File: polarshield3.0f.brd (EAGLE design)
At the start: 81.1 x 66 mm, 43 parts, among them Q4 BSS138, Q5 BSS138, Q6 BSS138, Q7 BSS138

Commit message: Added part number GF1A-E3/67A to D1, #1
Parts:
- D1: value (none) -> GF1A-E3/67A
- moved R9 6.00 mm to (23.0, 37.0)
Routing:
- net GND: track 316.7 -> 264.7 mm, vias 17 -> 13
- net M2_EN: track 82.8 -> 72.8 mm
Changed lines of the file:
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@@
 <attribute name="VALUE" x="32.73" y="60.46" size="1.27" layer="27"/>
 </element>
-<element name="D1" library="diode" package="DO214BA" value="" x="17.6" y="27" rot="R90"/>
+<element name="D1" library="diode" package="DO214BA" value="GF1A-E3/67A " x="17.6" y="27" rot="R90"/>
 <element name="MOTOR_2" library="sandy" package="A4988BREAKOUT" value="A4988BREAKOUT" x="20" y="52"/>
 <element name="SJ4" library="polargraph3" package="SJ_2S-NO" value="SOLDERJUMPERNO" x="27" y="43" smashed="yes" rot="MR270"/>
 <element name="SJ5" library="polargraph3" package="SJ_2S-TRACE" value="SOLDERJUMPERTRACE" x="24" y="43" smashed="yes" rot="MR270"/>
 <element name="SJ6" library="polargraph3" package="SJ_2S-TRACE" value="SOLDERJUMPERTRACE" x="21" y="43" smashed="yes" rot="MR270"/>
-<element name="R9" library="resistor" package="M0805" value="10k" x="29" y="37"/>
+<element name="R9" library="resistor" package="M0805" value="10k" x="23" y="37"/>
 <element name="C7" library="resistor" package="C0805" value="100nF" x="16" y="47" rot="R90"/>
 <element name="C8" library="resistor" package="153CLV-0605" value="100uF" x="23" y="47" rot="R180"/>
@@
 <wire x1="22.6" y1="49.8" x2="22.9" y2="49.8" width="1.27" layer="1"/>
 <wire x1="22.9" y1="49.8" x2="25.7" y2="47" width="1.27" layer="1"/>
-<wire x1="25.7" y1="47" x2="27.6" y2="47" width="1.27" layer="1"/>
-<wire x1="27.6" y1="47" x2="33.5" y2="47" width="1.27" layer="1"/>
-<wire x1="33.5" y1="47" x2="36.7" y2="50.2" width="1.27" layer="1"/>
-<wire x1="36.7" y1="50.2" x2="36.7" y2="53.08" width="1.27" layer="1"/>
-<wire x1="36.7" y1="53.08" x2="36.51" y2="53.27" width="1.27" layer="1"/>
 <wire x1="42" y1="47.95" x2="42" y2="53.1" width="1.27" layer="1"/>
 <wire x1="42" y1="53.1" x2="36.68" y2="53.1" width="1.27" layer="1"/>
@@
 <contactref element="CN2" pad="8"/>
 <contactref element="CN2" pad="4"/>
-<wire x1="24.125" y1="37.25" x2="23.875" y2="37" width="0.3048" layer="1"/>
-<wire x1="25.125" y1="37" x2="24.125" y2="37.25" width="0.3048" layer="1"/>
-<wire x1="20.125" y1="32" x2="25.125" y2="37" width="0.8128" layer="1"/>
-<wire x1="17" y1="32" x2="20.125" y2="32" width="0.3048" layer="1"/>
+<wire x1="17" y1="32" x2="20.125" y2="30" width="0.3048" layer="1"/>
 <wire x1="17" y1="34" x2="17" y2="32" width="0.3048" layer="1"/>
 <wire x1="17" y1="34" x2="16.95" y2="34" width="0.3048" layer="1"/>
@@
 <wire x1="19.9" y1="27.3" x2="20.125" y2="27.525" width="0.6096" layer="1"/>
 <wire x1="20.125" y1="27.525" x2="20.125" y2="28.2" width="0.6096" layer="1"/>
-<wire x1="20.125" y1="28.2" x2="20.125" y2="32" width="0.6096" layer="1"/>
+<wire x1="20.125" y1="28.2" x2="20.125" y2="30" width="0.6096" layer="1"/>
 <wire x1="27.28" y1="28.4" x2="27.08" y2="28.2" width="0.254" layer="16"/>
 <wire x1="27.08" y1="28.2" x2="20.125" y2="28.2" width="0.254" layer="16"/>
 <via x="20.125" y="28.2" extent="1-16" drill="0.3048"/>
-<via x="25" y="37" extent="1-16" drill="0.3048"/>
-<via x="35.3" y="38.5" extent="1-16" drill="0.3048"/>
-<wire x1="25.125" y1="37" x2="25" y2="37" width="0.254" layer="1"/>
-<wire x1="35.3" y1="38.5" x2="35.2" y2="38.6" width="0.254" layer="16"/>
-<wire x1="35.2" y1="38.6" x2="35.2" y2="46.1" width="0.254" layer="16"/>
-<wire x1="25" y1="37" x2="31.4" y2="37" width="0.254" layer="16"/>
-<via x="31.4" y="37" extent="1-16" drill="0.3048"/>
-<wire x1="31.4" y1="37" x2="33.8" y2="37" width="0.254" layer="1"/>
-<wire x1="33.8" y1="37" x2="35.3" y2="38.5" width="0.254" layer="1"/>
-<wire x1="35.2" y1="46.1" x2="34.7" y2="46.6" width="0.254" layer="16"/>
-<via x="34.7" y="46.6" extent="1-16" drill="0.3048"/>
-<wire x1="34.7" y1="46.6" x2="28" y2="46.6" width="0.254" layer="1"/>
-<wire x1="28" y1="46.6" x2="27.6" y2="47" width="0.254" layer="1"/>
 <contactref element="CN1" pad="8"/>
 <contactref element="CN1" pad="4"/>
@@
 <wire x1="33.0327" y1="63.0936" x2="32.95" y2="63" width="0.6096" layer="1"/>
 <wire x1="37.9476" y1="63.0936" x2="37.95" y2="63" width="0.6096" layer="1"/>
-<wire x1="30.0609" y1="38.8907" x2="30.0609" y2="37.0332" width="0.6096" layer="1"/>
-<wire x1="30.0609" y1="40.005" x2="30.0609" y2="38.8907" width="0.6096" layer="16"/>
-<wire x1="30.1752" y1="40.1193" x2="30.0609" y2="40.005" width="0.6096" layer="16"/>
-<wire x1="30.1752" y1="41.148" x2="30.1752" y2="40.1193" width="0.6096" layer="16"/>
-<wire x1="27.8892" y1="43.434" x2="30.1752" y2="41.148" width="0.6096" layer="16"/>
 <wire x1="27.3177" y1="43.434" x2="27.8892" y2="43.434" width="0.6096" layer="16"/>
-<wire x1="30.0609" y1="37.0332" x2="29.95" y2="37" width="0.6096" layer="1"/>
 <wire x1="27.3177" y1="43.434" x2="27" y2="43.45" width="0.6096" layer="16"/>
 <wire x1="37.8333" y1="62.7507" x2="37.95" y2="63" width="0.6096" layer="1"/>
@@
 <wire x1="34.1757" y1="53.0352" x2="33.97" y2="53.27" width="0.6096" layer="16"/>
 <wire x1="60.6933" y1="53.1495" x2="60.97" y2="53.27" width="0.6096" layer="16"/>
-<via x="30.0609" y="38.8907" extent="1-16" drill="0.3048"/>
 <contactref element="Q4" pad="1"/>
 <contactref element="Q5" pad="1"/>
@@
 <wire x1="36.2" y1="9.2" x2="36.2" y2="9.0331" width="0.254" layer="1"/>
 <wire x1="36.2" y1="9.0331" x2="36.2331" y2="9" width="0.254" layer="1"/>
-<wire x1="21" y1="43.508" x2="24" y2="43.508" width="0.4064" layer="16"/>
+<wire x1="21" y1="43.508" x2="22.4" y2="43.508" width="0.4064" layer="16"/>
+<wire x1="22.4" y1="43.508" x2="24" y2="43.508" width="0.4064" layer="16"/>
 <wire x1="24" y1="43.508" x2="27" y2="43.508" width="0.4064" layer="16"/>
 <wire x1="27" y1="43.508" x2="27" y2="43.45" width="0.4064" layer="16"/>
@@
 <wire x1="5.3" y1="17.89" x2="6.54" y2="16.65" width="0.3048" layer="1"/>
 <wire x1="8.875" y1="29.145" x2="6.54" y2="26.81" width="0.6096" layer="1"/>
+<wire x1="23.95" y1="37" x2="23.95" y2="38.15" width="0.4064" layer="1"/>
+<wire x1="23.95" y1="38.15" x2="23.4" y2="38.7" width="0.4064" layer="1"/>
+<wire x1="23.4" y1="38.7" x2="22.5" y2="38.7" width="0.4064" layer="1"/>
+<via x="22.5" y="38.7" extent="1-16" drill="0.6" shape="square"/>
+<wire x1="22.5" y1="38.7" x2="22.5" y2="43.408" width="0.4064" layer="16"/>
+<wire x1="22.5" y1="43.408" x2="22.4" y2="43.508" width="0.4064" layer="16"/>
 </signal>
 <signal name="M1_EN">
@@
 <contactref element="MOTOR_2" pad="EN"/>
 <contactref element="R9" pad="1"/>
-<wire x1="26.9461" y1="37.0332" x2="28.0035" y2="37.0332" width="0.254" layer="1"/>
-<wire x1="25.9458" y1="38.7335" x2="26.9" y2="37.8" width="0.254" layer="1"/>
-<wire x1="26.9" y1="37.8" x2="26.9461" y2="37.7539" width="0.254" layer="1" curve="-90"/>
-<wire x1="26.9461" y1="37.7539" x2="26.9461" y2="37.0332" width="0.254" layer="1"/>
-<wire x1="23.6315" y1="38.7335" x2="25.9458" y2="38.7335" width="0.254" layer="1"/>
-<wire x1="22.7028" y1="39.6622" x2="23.6315" y2="38.7335" width="0.254" layer="1"/>
-<wire x1="22.7028" y1="40.9194" x2="22.7028" y2="39.6622" width="0.254" layer="1"/>
-<wire x1="22.017" y1="41.6052" x2="22.7028" y2="40.9194" width="0.254" layer="1"/>
-<wire x1="19.7739" y1="41.6052" x2="22.017" y2="41.6052" width="0.254" layer="1"/>
-<wire x1="18.7452" y1="40.5765" x2="19.7739" y2="41.6052" width="0.254" layer="1"/>
-<wire x1="28.0035" y1="37.0332" x2="28.05" y2="37" width="0.254" layer="1"/>
-<wire x1="18.7452" y1="40.5765" x2="18.73" y2="40.57" width="0.254" layer="1"/>
 <wire x1="62.7507" y1="8.4582" x2="62.7507" y2="3.0861" width="0.254" layer="1"/>
 <wire x1="56.007" y1="15.2019" x2="62.7507" y2="8.4582" width="0.254" layer="1"/>
@@
 <wire x1="21.2885" y1="23.2316" x2="26.2321" y2="18.288" width="0.254" layer="1"/>
 <wire x1="21.2885" y1="31.2613" x2="21.2885" y2="23.2316" width="0.254" layer="1"/>
-<wire x1="26.9461" y1="37.0332" x2="26.9461" y2="36.9" width="0.254" layer="1"/>
-<wire x1="26.9461" y1="36.9" x2="25.6" y2="35.6" width="0.254" layer="1"/>
-<wire x1="25.6" y1="35.6" x2="21.2885" y2="31.2613" width="0.254" layer="1"/>
 <wire x1="62.7507" y1="3.0861" x2="62.84" y2="3" width="0.254" layer="1"/>
+<wire x1="18.73" y1="40.57" x2="18.73" y2="40.32" width="0.4064" layer="1"/>
+<wire x1="18.73" y1="40.32" x2="22.05" y2="37" width="0.4064" layer="1"/>
+<wire x1="21.2885" y1="31.2613" x2="21.2885" y2="36.2385" width="0.4064" layer="1"/>
+<wire x1="21.2885" y1="36.2385" x2="22.05" y2="37" width="0.4064" layer="1"/>
 </signal>
 <signal name="M2_STEP">

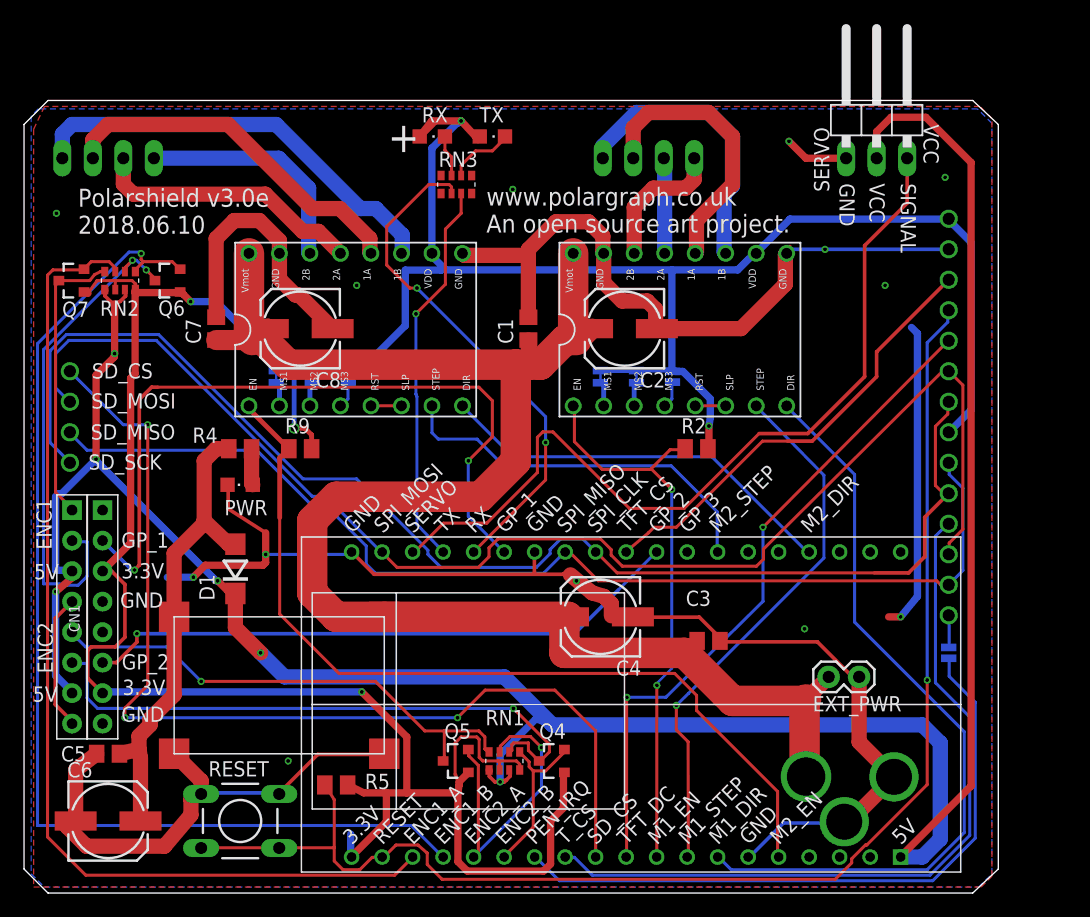
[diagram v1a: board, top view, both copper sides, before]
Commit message: v3.0f. Removed 1k resistors, moved motor connectors and pads for mini-360.
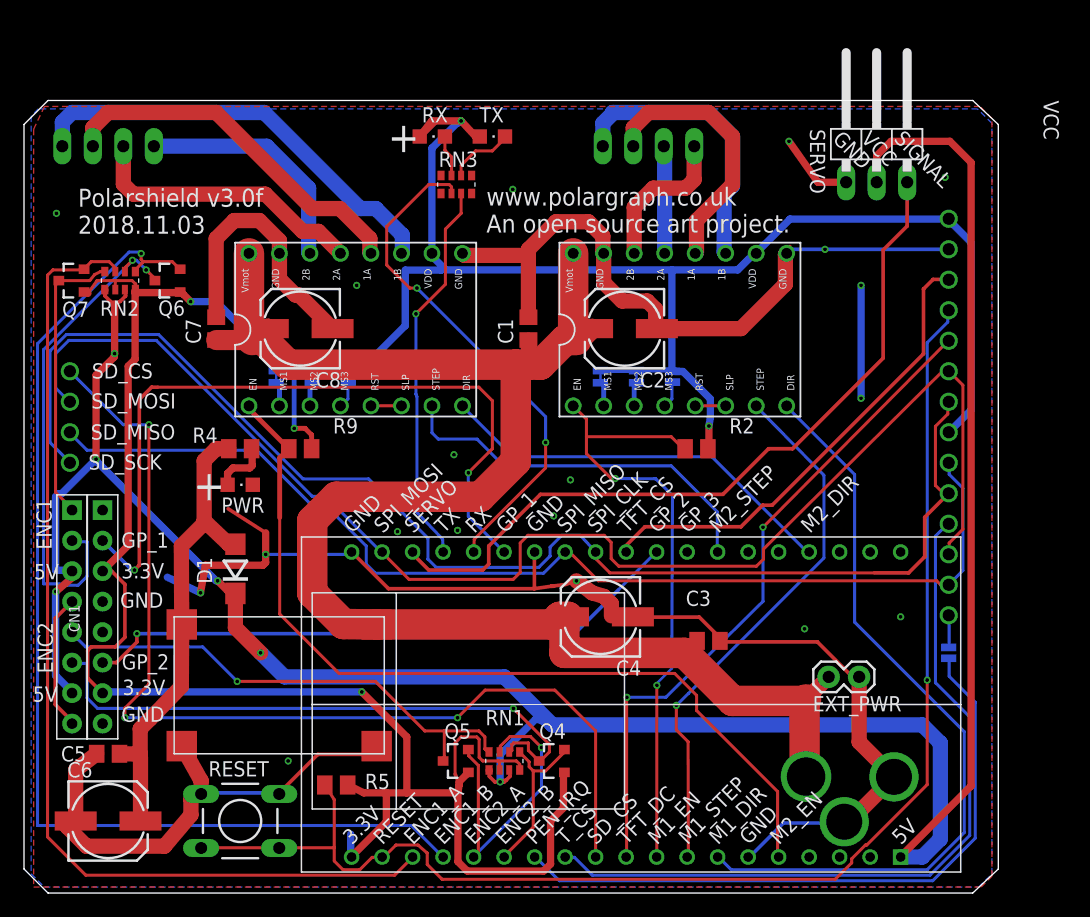
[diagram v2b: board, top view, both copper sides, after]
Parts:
- U$3: value MINI-360-MP2307 -> MINI-360-MP2307MINI-360-MP2307_T
- moved SERVO 2.00 mm to (71.0, 63.0)
- moved M1_CONN 1.00 mm to (52.0, 66.0)
- moved M2_CONN 1.00 mm to (7.00, 66.0)
- turned PWR to 270 degrees
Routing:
- net GND: track 264.7 -> 251.6 mm, vias 13 -> 19
- net SERVO1: track 70.3 -> 63.6 mm
- net M1_EN: track 47.5 -> 52.2 mm
- net SPI_MOSI: track 113.2 -> 115.8 mm
- net TFT_CS: track 37.5 -> 39.9 mm
- net SPI_CLK: track 110.0 -> 111.6 mm
- net N$8: track 3.04 -> 4.69 mm
- net N$21: track 22.6 -> 23.6 mm
- net N$12: track 23.2 -> 22.2 mm
- net N$10: track 11.6 -> 12.6 mm
- net N$11: track 7.95 -> 8.92 mm
- net +5V: track 218.8 -> 218.0 mm
- net +12V: track 148.3 -> 148.8 mm
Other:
- board text added: "An open source art project. v3.0f"
- board text added: "PolargraphSD."
- board text added: "Polarshield v3.0f 2018.11.03"
- board text removed: "An open source art project. 2018.06.10"
- board text removed: "Polarshield v3.0e 2018.06.10"
- board text removed: "www.polargraph.co.uk"

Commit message: v3.1 changed servo supply voltage to 3.3v
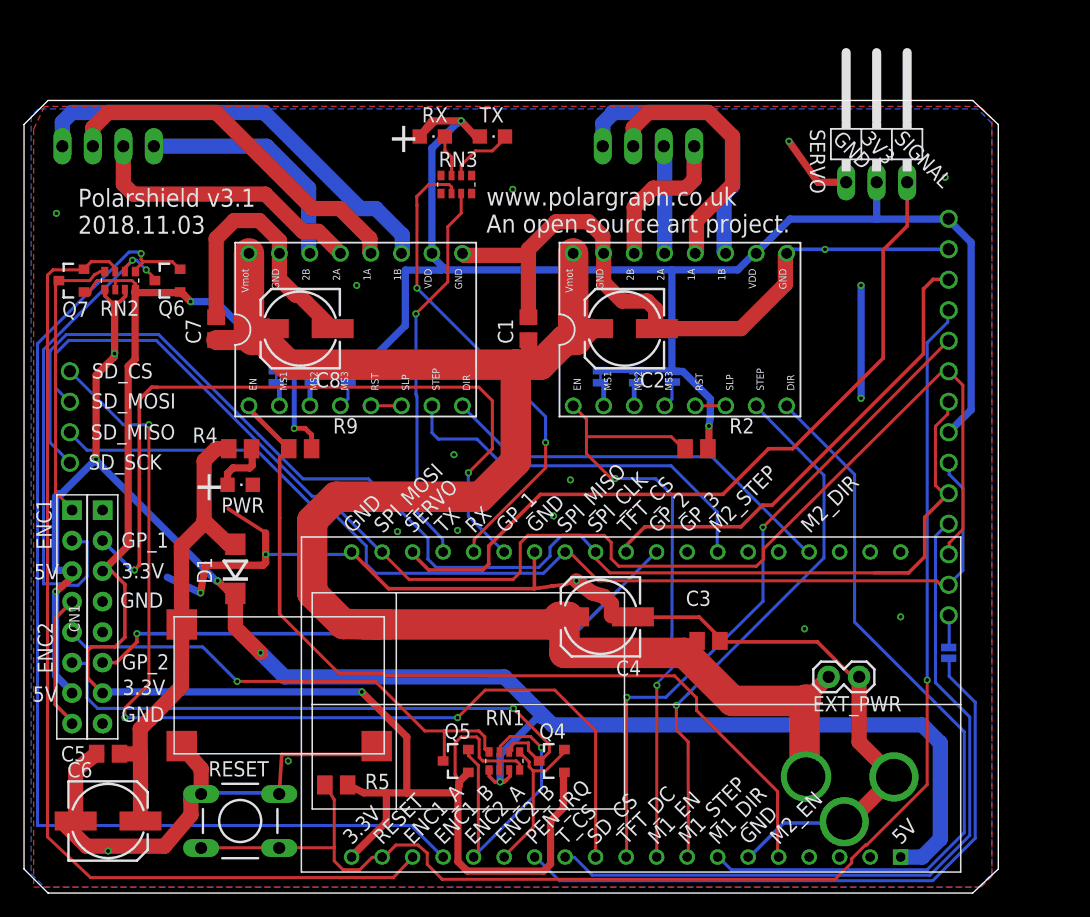
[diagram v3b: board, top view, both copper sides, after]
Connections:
- net +3V3: now also SERVO.2
- net +5V: no longer SERVO.2
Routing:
- net +5V: track 218.0 -> 146.4 mm
- net RX: track 42.9 -> 40.4 mm
- net GND: track 251.6 -> 253.5 mm, vias 19 -> 20
- net +3V3: track 282.8 -> 284.0 mm
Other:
- board text added: "3V3"
- board text added: "An open source art project. v3.1"
- board text added: "Polarshield v3.1 2018.11.03"
- board text removed: "An open source art project. v3.0f"
- board text removed: "Polarshield v3.0f 2018.11.03"
